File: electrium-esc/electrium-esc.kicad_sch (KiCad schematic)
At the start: 21 parts

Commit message: Fix Error
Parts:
- added TP1: M_1A, symbol Connector:TestPoint_Small
- added TP2: M_2A, symbol Connector:TestPoint_Small
- added TP3: M_3A, symbol Connector:TestPoint_Small
- added TP4: M_1B, symbol Connector:TestPoint_Small
- added TP5: M_2B, symbol Connector:TestPoint_Small
- added TP6: M_3B, symbol Connector:TestPoint_Small
- C1: renamed from C?; footprint (none) -> Capacitor_SMD:C_0603_1608Metric
- D1, D2: renamed from D?; footprint (none) -> Diode_SMD:D_0201_0603Metric
- J1, J4: renamed from J?; footprint (none) -> Connector_PinHeader_2.54mm:PinHeader_1x04_P2.54mm_Horizontal
- J3: renamed from J?; footprint (none) -> Connector_PinHeader_2.54mm:PinHeader_1x03_P2.54mm_Vertical_SMD_Pin1Right
- R1, R10, R2, R3, R4, R5, R6, R7, R8, R9: renamed from R?; footprint (none) -> Resistor_SMD:R_0603_1608Metric
- R11, R12, R13, R14: renamed from R?; footprint (none) -> Resistor_SMD:R_Shunt_Ohmite_LVK12
- gave numbers to parts that had none: 1
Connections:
- net Power MOSFETs/Phase_1: now also TP1.1
- net Power MOSFETs/Phase_2: now also TP2.1
- net Power MOSFETs/Phase_3: now also TP3.1
- net Power MOSFETs1/Phase_1: now also TP4.1
- net Power MOSFETs1/Phase_2: now also TP5.1
- net Power MOSFETs1/Phase_3: now also TP6.1

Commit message: Update Footprints for schematic symbols
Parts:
- J2: footprint MOLEX_1050170001 -> 1050170001:MOLEX_1050170001
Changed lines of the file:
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@@
     (property "Reference" "J2" (id 0) (at 43.18 46.99 0))
     (property "Value" "1050170001" (id 1) (at 44.45 71.12 0))
-    (property "Footprint" "MOLEX_1050170001" (id 2) (at 43.18 58.42 0)
+    (property "Footprint" "1050170001:MOLEX_1050170001" (id 2) (at 43.18 58.42 0)
       (effects (font (size 1.27 1.27)) (justify bottom) hide)
     )
@@
     )
     (path "/d5a4fada-a18a-42a3-b0ea-f163f0770a26"
-      (reference "J2") (unit 1) (value "1050170001") (footprint "MOLEX_1050170001")
+      (reference "J2") (unit 1) (value "1050170001") (footprint "1050170001:MOLEX_1050170001")
     )
     (path "/9797036c-f702-4f5f-bef1-41a9950c6932"
@@
     )
     (path "/95515899-f309-4706-b478-ef0c1d74de3d/764763fd-5dd9-4c52-a8c3-a0c0d2fc9a51"
-      (reference "PS1") (unit 1) (value "TC2117-3.3VDBTR") (footprint "SOT230P700X180-4N")
+      (reference "PS1") (unit 1) (value "TC2117-3.3VDBTR") (footprint "Package_TO_SOT_SMD:SOT-223")
     )
     (path "/9cfb263a-ea56-4cbe-86e2-b1fdf4c95ad6/d53fb4d6-fc01-4087-95e0-8b15cdc15d7a"
@@
     )
     (path "/4dcd2554-0c0c-4fca-b220-d2fb156d9cf9/b9bd665f-b20d-4cd0-b6ff-e6534d047e07"
-      (reference "U2") (unit 1) (value "DRV8301DCAR") (footprint "SOP50P810X120-57N")
+      (reference "U2") (unit 1) (value "DRV8301DCAR") (footprint "Package_SO:HTSSOP-56-1EP_6.1x14mm_P0.5mm_EP3.61x6.35mm")
     )
     (path "/f169605c-998e-4bf3-977e-b281c665fab8/28a16657-974d-453b-b6c0-41dddf93c2c8"
@@
     )
     (path "/8c1d7bfe-a7ad-4b08-9e6d-dd7b239bc0ed/b9bd665f-b20d-4cd0-b6ff-e6534d047e07"
-      (reference "U4") (unit 1) (value "DRV8301DCAR") (footprint "SOP50P810X120-57N")
+      (reference "U4") (unit 1) (value "DRV8301DCAR") (footprint "Package_SO:HTSSOP-56-1EP_6.1x14mm_P0.5mm_EP3.61x6.35mm")
     )
     (path "/9d2b8e53-abda-48f4-a6e0-4b62c24d8218/aa2bd1cf-a201-4778-9291-e88119c53fa2"

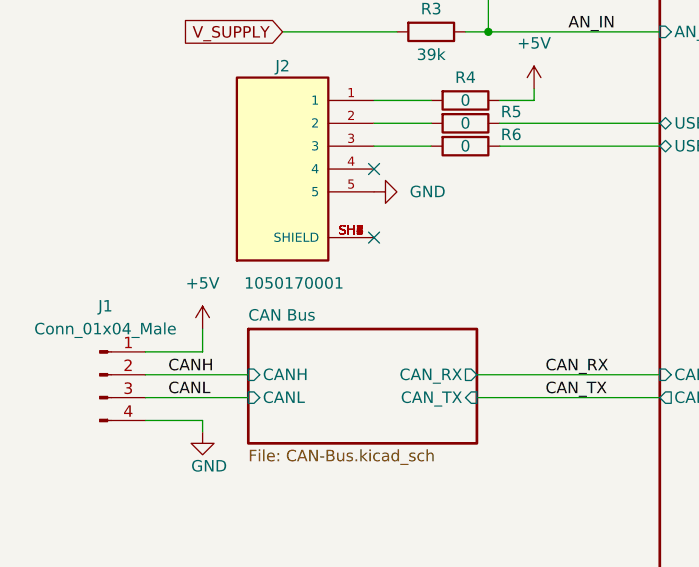
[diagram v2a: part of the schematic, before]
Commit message: Create motor pad footprint
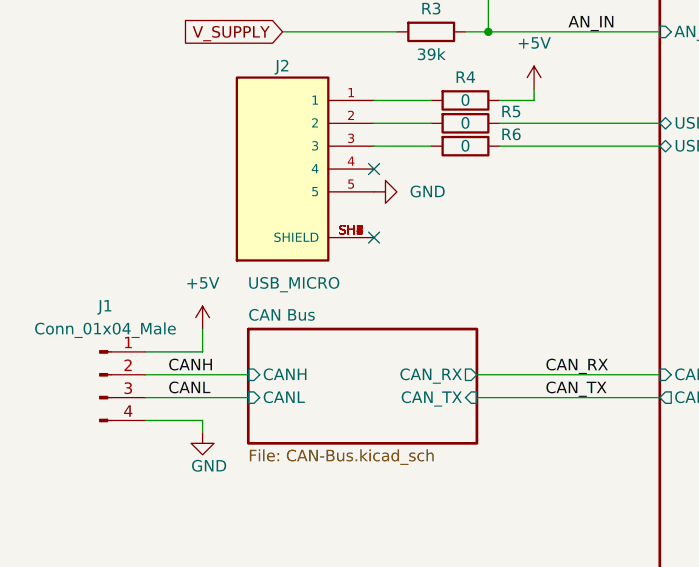
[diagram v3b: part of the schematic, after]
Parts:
- J2: value 1050170001 -> USB_MICRO
- TP1, TP2, TP3, TP4, TP5, TP6: footprint (none) -> MOTOR:MOTOR_PAD
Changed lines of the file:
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@@
       (effects (font (size 1.27 1.27)) (justify left))
     )
-    (property "Footprint" "" (id 2) (at 267.97 54.61 0)
+    (property "Footprint" "MOTOR:MOTOR_PAD" (id 2) (at 267.97 54.61 0)
       (effects (font (size 1.27 1.27)) hide)
     )
@@
       (effects (font (size 1.27 1.27)) (justify left))
     )
-    (property "Footprint" "" (id 2) (at 267.97 78.74 0)
+    (property "Footprint" "MOTOR:MOTOR_PAD" (id 2) (at 267.97 78.74 0)
       (effects (font (size 1.27 1.27)) hide)
     )
@@
       (effects (font (size 1.27 1.27)) (justify left))
     )
-    (property "Footprint" "" (id 2) (at 267.97 116.84 0)
+    (property "Footprint" "MOTOR:MOTOR_PAD" (id 2) (at 267.97 116.84 0)
       (effects (font (size 1.27 1.27)) hide)
     )
@@
       (effects (font (size 1.27 1.27)) (justify left))
     )
-    (property "Footprint" "" (id 2) (at 267.97 140.97 0)
+    (property "Footprint" "MOTOR:MOTOR_PAD" (id 2) (at 267.97 140.97 0)
       (effects (font (size 1.27 1.27)) hide)
     )
@@
       (effects (font (size 1.27 1.27)) (justify left))
     )
-    (property "Footprint" "" (id 2) (at 267.97 128.27 0)
+    (property "Footprint" "MOTOR:MOTOR_PAD" (id 2) (at 267.97 128.27 0)
       (effects (font (size 1.27 1.27)) hide)
     )
@@
       (effects (font (size 1.27 1.27)) (justify left))
     )
-    (property "Footprint" "" (id 2) (at 267.97 66.04 0)
+    (property "Footprint" "MOTOR:MOTOR_PAD" (id 2) (at 267.97 66.04 0)
       (effects (font (size 1.27 1.27)) hide)
     )
@@
     (in_bom yes) (on_board yes)
     (property "Reference" "J2" (id 0) (at 43.18 46.99 0))
-    (property "Value" "1050170001" (id 1) (at 44.45 71.12 0))
+    (property "Value" "USB_MICRO" (id 1) (at 44.45 71.12 0))
     (property "Footprint" "1050170001:MOLEX_1050170001" (id 2) (at 43.18 58.42 0)
       (effects (font (size 1.27 1.27)) (justify bottom) hide)
@@
     )
     (path "/d5a4fada-a18a-42a3-b0ea-f163f0770a26"
-      (reference "J2") (unit 1) (value "1050170001") (footprint "1050170001:MOLEX_1050170001")
+      (reference "J2") (unit 1) (value "USB_MICRO") (footprint "1050170001:MOLEX_1050170001")
     )
     (path "/9797036c-f702-4f5f-bef1-41a9950c6932"
@@
     )
     (path "/1103bf25-eb3b-4b5f-be90-ee73f5756e8c"
-      (reference "TP1") (unit 1) (value "M_1A") (footprint "")
+      (reference "TP1") (unit 1) (value "M_1A") (footprint "MOTOR:MOTOR_PAD")
     )
     (path "/c97bb9b7-1a01-4d55-8c14-fddf7e222b68"
-      (reference "TP2") (unit 1) (value "M_2A") (footprint "")
+      (reference "TP2") (unit 1) (value "M_2A") (footprint "MOTOR:MOTOR_PAD")
     )
     (path "/34224e78-6cdd-43c9-9eb8-edd7dd9f2bb8"
-      (reference "TP3") (unit 1) (value "M_3A") (footprint "")
+      (reference "TP3") (unit 1) (value "M_3A") (footprint "MOTOR:MOTOR_PAD")
     )
     (path "/4cc05b63-50f5-486f-aef4-bbbf0637bd1f"
-      (reference "TP4") (unit 1) (value "M_1B") (footprint "")
+      (reference "TP4") (unit 1) (value "M_1B") (footprint "MOTOR:MOTOR_PAD")
     )
     (path "/adc79ce8-d506-4352-8fbb-fb0703500f6d"
-      (reference "TP5") (unit 1) (value "M_2B") (footprint "")
+      (reference "TP5") (unit 1) (value "M_2B") (footprint "MOTOR:MOTOR_PAD")
     )
     (path "/8bc4dbf2-78bc-4da9-b471-48c8d0871757"
-      (reference "TP6") (unit 1) (value "M_3B") (footprint "")
+      (reference "TP6") (unit 1) (value "M_3B") (footprint "MOTOR:MOTOR_PAD")
     )
     (path "/95515899-f309-4706-b478-ef0c1d74de3d/817b9562-8e7c-44fd-a0ab-5d22e23884af"

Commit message: Update footprints
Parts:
- J1, J4: footprint Connector_PinHeader_2.54mm:PinHeader_1x04_P2.54mm_Horizontal -> Connector_PinHeader_2.54mm:PinHeader_1x04_P2.54mm_Vertical
- J2: footprint 1050170001:MOLEX_1050170001 -> USB_MICRO:MOLEX_1050170001
- J3: footprint Connector_PinHeader_2.54mm:PinHeader_1x03_P2.54mm_Vertical_SMD_Pin1Right -> Connector_PinHeader_2.54mm:PinHeader_1x03_P2.54mm_Vertical
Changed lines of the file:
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@@
     (property "Reference" "J1" (id 0) (at 23.495 73.66 0))
     (property "Value" "Conn_01x04_Male" (id 1) (at 23.495 76.2 0))
-    (property "Footprint" "Connector_PinHeader_2.54mm:PinHeader_1x04_P2.54mm_Horizontal" (id 2) (at 22.86 81.28 0)
+    (property "Footprint" "Connector_PinHeader_2.54mm:PinHeader_1x04_P2.54mm_Vertical" (id 2) (at 22.86 81.28 0)
       (effects (font (size 1.27 1.27)) hide)
     )
@@
     (property "Reference" "J4" (id 0) (at 167.64 187.96 90))
     (property "Value" "Conn_01x04_Male" (id 1) (at 167.64 190.5 90))
-    (property "Footprint" "Connector_PinHeader_2.54mm:PinHeader_1x04_P2.54mm_Horizontal" (id 2) (at 166.37 185.42 0)
+    (property "Footprint" "Connector_PinHeader_2.54mm:PinHeader_1x04_P2.54mm_Vertical" (id 2) (at 166.37 185.42 0)
       (effects (font (size 1.27 1.27)) hide)
     )
@@
     (property "Reference" "J3" (id 0) (at 53.34 156.21 0))
     (property "Value" "Conn_01x03_Male" (id 1) (at 53.34 158.75 0))
-    (property "Footprint" "Connector_PinHeader_2.54mm:PinHeader_1x03_P2.54mm_Vertical_SMD_Pin1Right" (id 2) (at 58.42 163.83 0)
+    (property "Footprint" "Connector_PinHeader_2.54mm:PinHeader_1x03_P2.54mm_Vertical" (id 2) (at 58.42 163.83 0)
       (effects (font (size 1.27 1.27)) hide)
     )
@@
     (property "Reference" "J2" (id 0) (at 43.18 46.99 0))
     (property "Value" "USB_MICRO" (id 1) (at 44.45 71.12 0))
-    (property "Footprint" "1050170001:MOLEX_1050170001" (id 2) (at 43.18 58.42 0)
+    (property "Footprint" "USB_MICRO:MOLEX_1050170001" (id 2) (at 43.18 58.42 0)
       (effects (font (size 1.27 1.27)) (justify bottom) hide)
     )
@@
     )
     (path "/4dcd2554-0c0c-4fca-b220-d2fb156d9cf9/9b6e504a-823b-4004-a68a-5c4b78b4c3aa"
-      (reference "C41") (unit 1) (value "47u") (footprint "Capacitor_THT:CP_Radial_D10.0mm_P5.00mm")
+      (reference "C41") (unit 1) (value "47u") (footprint "Capacitor_THT:CP_Radial_D4.0mm_P1.50mm")
     )
     (path "/4dcd2554-0c0c-4fca-b220-d2fb156d9cf9/738b00ae-51e0-4d5a-ab67-667b75c1dfa5"
@@
     )
     (path "/8c1d7bfe-a7ad-4b08-9e6d-dd7b239bc0ed/9b6e504a-823b-4004-a68a-5c4b78b4c3aa"
-      (reference "C67") (unit 1) (value "47u") (footprint "Capacitor_THT:CP_Radial_D10.0mm_P5.00mm")
+      (reference "C67") (unit 1) (value "47u") (footprint "Capacitor_THT:CP_Radial_D4.0mm_P1.50mm")
     )
     (path "/8c1d7bfe-a7ad-4b08-9e6d-dd7b239bc0ed/738b00ae-51e0-4d5a-ab67-667b75c1dfa5"
@@
     )
     (path "/9d2b8e53-abda-48f4-a6e0-4b62c24d8218/a33ccc0b-45e6-4e7b-ac1d-521d7520e388"
-      (reference "C77") (unit 1) (value "47u") (footprint "Capacitor_THT:CP_Radial_D10.0mm_P5.00mm")
+      (reference "C77") (unit 1) (value "47u") (footprint "Capacitor_THT:CP_Radial_D4.0mm_P1.50mm")
     )
     (path "/5098eb75-ab3f-49e8-b692-4372bb393d18"
@@
     )
     (path "/7b58be21-461d-4602-87a2-ef9eb645ff28"
-      (reference "J1") (unit 1) (value "Conn_01x04_Male") (footprint "Connector_PinHeader_2.54mm:PinHeader_1x04_P2.54mm_Horizontal")
+      (reference "J1") (unit 1) (value "Conn_01x04_Male") (footprint "Connector_PinHeader_2.54mm:PinHeader_1x04_P2.54mm_Vertical")
     )
     (path "/d5a4fada-a18a-42a3-b0ea-f163f0770a26"
-      (reference "J2") (unit 1) (value "USB_MICRO") (footprint "1050170001:MOLEX_1050170001")
+      (reference "J2") (unit 1) (value "USB_MICRO") (footprint "USB_MICRO:MOLEX_1050170001")
     )
     (path "/9797036c-f702-4f5f-bef1-41a9950c6932"
-      (reference "J3") (unit 1) (value "Conn_01x03_Male") (footprint "Connector_PinHeader_2.54mm:PinHeader_1x03_P2.54mm_Vertical_SMD_Pin1Right")
+      (reference "J3") (unit 1) (value "Conn_01x03_Male") (footprint "Connector_PinHeader_2.54mm:PinHeader_1x03_P2.54mm_Vertical")
     )
     (path "/928f53cb-3848-4c94-9638-22c4359c3f9a"
-      (reference "J4") (unit 1) (value "Conn_01x04_Male") (footprint "Connector_PinHeader_2.54mm:PinHeader_1x04_P2.54mm_Horizontal")
+      (reference "J4") (unit 1) (value "Conn_01x04_Male") (footprint "Connector_PinHeader_2.54mm:PinHeader_1x04_P2.54mm_Vertical")
     )
     (path "/95515899-f309-4706-b478-ef0c1d74de3d/ab272a38-ae91-43cc-8c37-b105b22f7c71"
-      (reference "J5") (unit 1) (value "Debug Connector") (footprint "Connector_PinHeader_2.54mm:PinHeader_1x06_P2.54mm_Horizontal")
+      (reference "J5") (unit 1) (value "Debug Connector") (footprint "Connector_PinHeader_2.54mm:PinHeader_1x06_P2.54mm_Vertical")
     )
     (path "/4dcd2554-0c0c-4fca-b220-d2fb156d9cf9/ff64180e-b6ce-40be-a953-e6a02ff559dd"

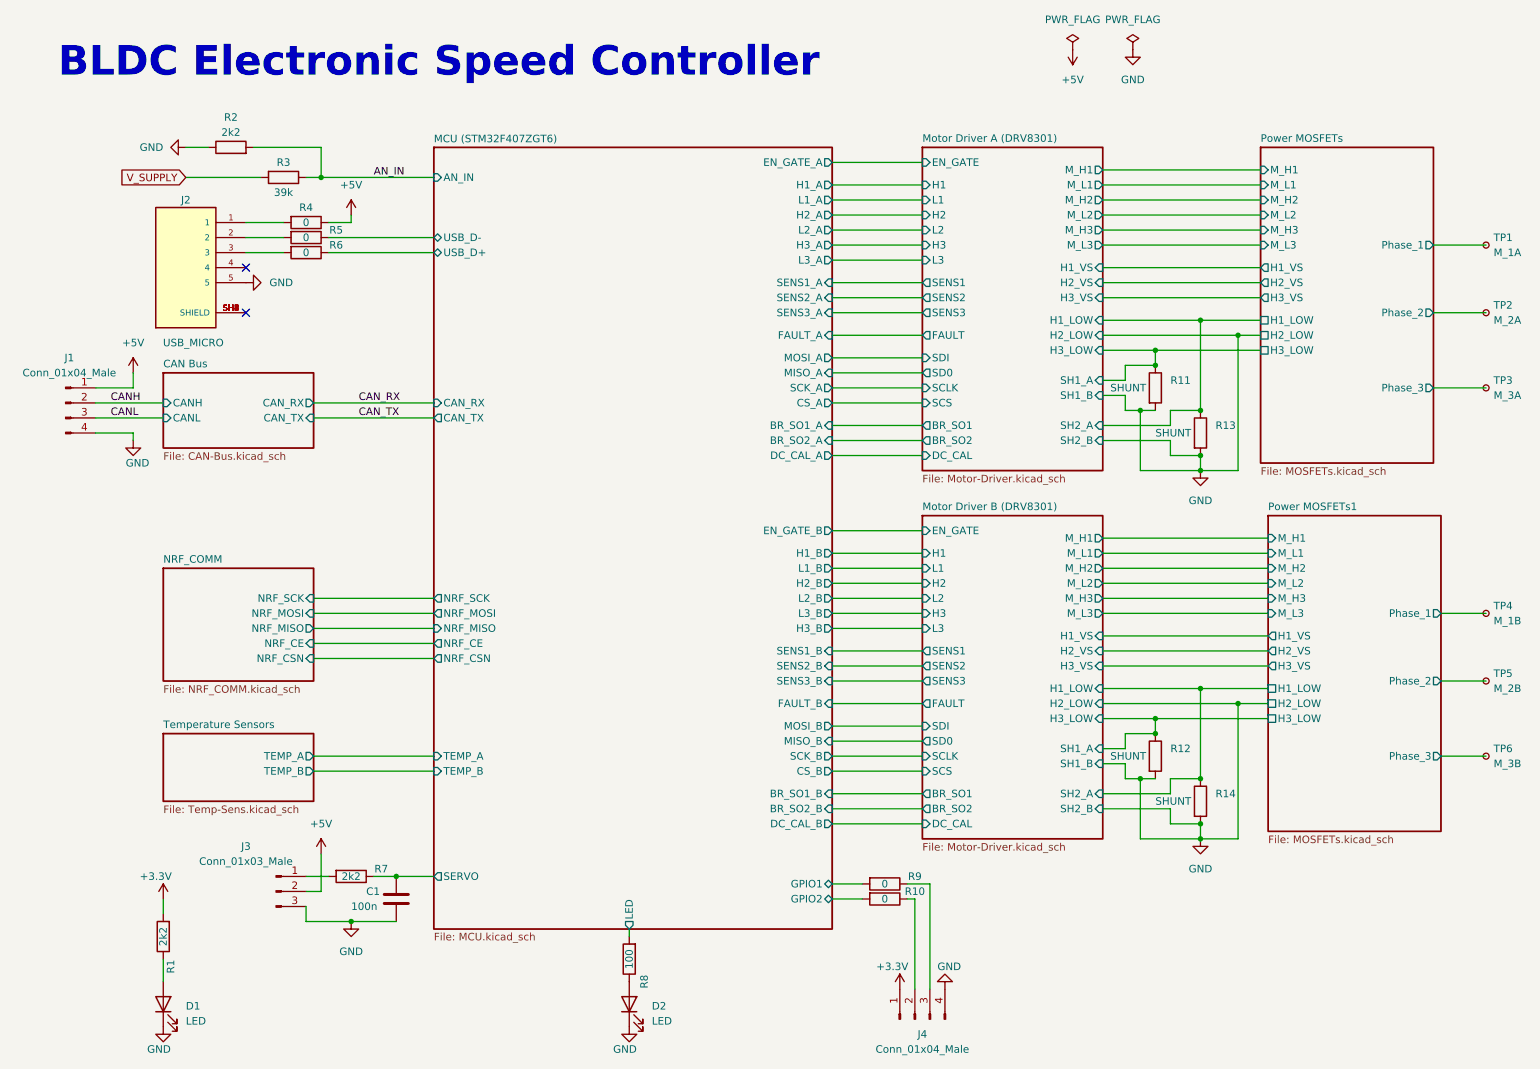
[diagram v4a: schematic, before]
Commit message: relabel components to make more sense
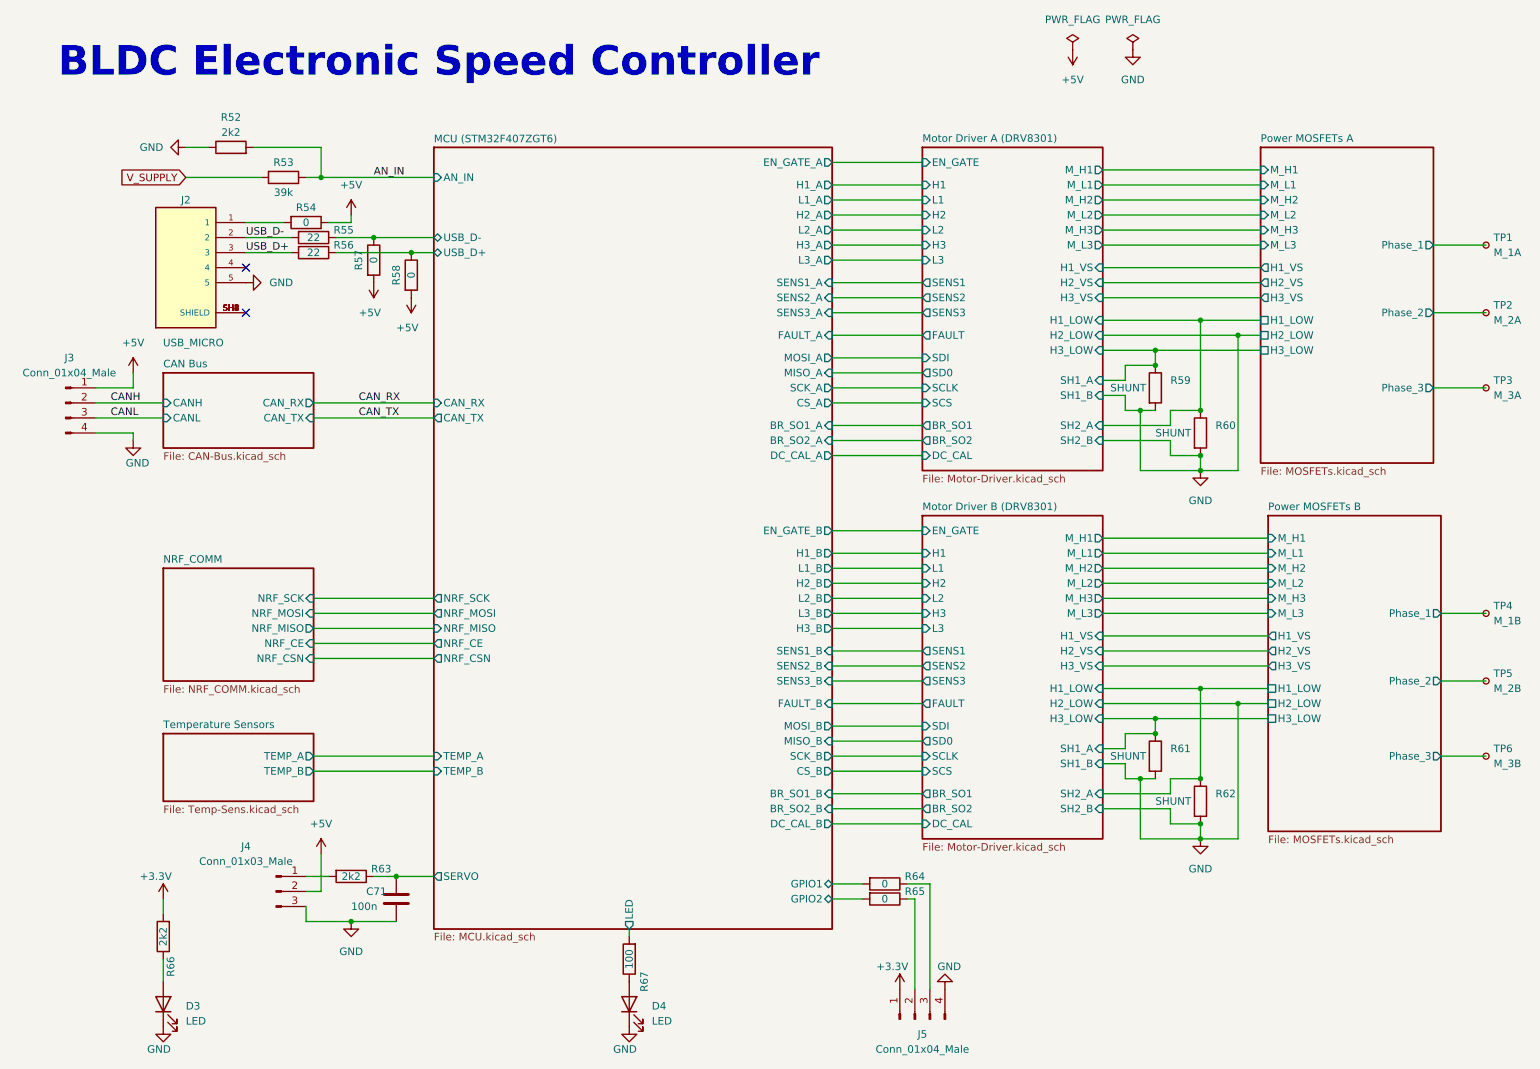
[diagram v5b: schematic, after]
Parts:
- added R57, R58: 0, Resistor_SMD:R_0603_1608Metric, symbol Device:R
- R55: renamed from R5; value 0 -> 22
- R56: renamed from R6; value 0 -> 22
- renumbered C1 to C71, D1 to D3, D2 to D4, J1 to J3, J3 to J4, J4 to J5, R2 to R52, R3 to R53, R4 to R54, R11 to R59, R13 to R60, R12 to R61, R14 to R62, R7 to R63, R9 to R64, R10 to R65, R1 to R66, R8 to R67
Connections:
- net +5V: now also R57.2, R58.2
- net MCU (STM32F407ZGT6)/USB_D+: now also R58.1
- net MCU (STM32F407ZGT6)/USB_D-: now also R57.1
- net USB_D+: now reaches J2.3, R56.2
- net USB_D-: now reaches J2.2, R55.2
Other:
- sheet Power MOSFETs renamed Power MOSFETs A
- sheet Power MOSFETs1 renamed Power MOSFETs B
- moved on the sheet: R55, R56
